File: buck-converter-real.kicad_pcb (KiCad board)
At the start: 4 copper layers, 64 x 64 mm, 75 parts, among them J1 Conn_01x02_Pin, J1 USB_C_Receptacle_USB2.0_16P, J10 I2C1, J12 Conn_01x04, J13 Conn_01x12, J2 SOL 24V, J3 Battery out (3V6-4V2) NiMH 3S, J5 Barrel_Jack_MountingPin, J6 DM3CS-SF, J7 UART 1, J8 I2C1, J9 SWD, Q2 CSD18540Q5B - 60-V, SW2 SW_Omron_B3FS, U1 AP2112K-3.3 (3V3 LDO), U2 CH32V203K8T6, U5 LM5109BMA (Mosfet Driver), U6 78L12L (12V LDO) (35V max), Y1 8MHz 20pF

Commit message: Update layout
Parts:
- added REF**: Untitled, forest-ch:Untitled, F.Cu at (113.8, 70.5)
- added REF**1: Untitled, forest-ch:Untitled, F.Cu at (116.4, 70.5)
- added REF**10: Untitled, forest-ch:Untitled, F.Cu at (124.0, 73.1)
- added REF**12: Untitled, forest-ch:Untitled, F.Cu at (113.8, 75.6)
- added REF**13: Untitled, forest-ch:Untitled, F.Cu at (116.4, 75.6)
- added REF**14: Untitled, forest-ch:Untitled, F.Cu at (118.9, 75.6)
- added REF**15: Untitled, forest-ch:Untitled, F.Cu at (121.5, 75.6)
- added REF**16: Untitled, forest-ch:Untitled, F.Cu at (124.0, 75.6)
- added REF**17: Untitled, forest-ch:Untitled, F.Cu at (126.5, 75.6)
- added REF**18: Untitled, forest-ch:Untitled, F.Cu at (113.8, 78.2)
- added REF**19: Untitled, forest-ch:Untitled, F.Cu at (116.4, 78.2)
- added REF**2: Untitled, forest-ch:Untitled, F.Cu at (118.9, 70.5)
- added REF**20: Untitled, forest-ch:Untitled, F.Cu at (118.9, 78.2)
- added REF**21: Untitled, forest-ch:Untitled, F.Cu at (121.5, 78.2)
- added REF**22: Untitled, forest-ch:Untitled, F.Cu at (124.0, 78.2)
- added REF**23: Untitled, forest-ch:Untitled, F.Cu at (126.5, 78.2)
- added REF**24: Untitled, forest-ch:Untitled, F.Cu at (113.8, 80.7)
- added REF**25: Untitled, forest-ch:Untitled, F.Cu at (116.4, 80.7)
- added REF**26: Untitled, forest-ch:Untitled, F.Cu at (118.9, 80.7)
- added REF**27: Untitled, forest-ch:Untitled, F.Cu at (121.5, 80.7)
- added REF**28: Untitled, forest-ch:Untitled, F.Cu at (124.0, 80.7)
- added REF**29: Untitled, forest-ch:Untitled, F.Cu at (126.5, 80.7)
- added REF**3: Untitled, forest-ch:Untitled, F.Cu at (121.5, 70.5)
- added REF**30: Untitled, forest-ch:Untitled, F.Cu at (113.8, 83.2)
- added REF**31: Untitled, forest-ch:Untitled, F.Cu at (116.4, 83.2)
- added REF**32: Untitled, forest-ch:Untitled, F.Cu at (118.9, 83.2)
- added REF**33: Untitled, forest-ch:Untitled, F.Cu at (121.5, 83.2)
- added REF**34: Untitled, forest-ch:Untitled, F.Cu at (124.0, 83.2)
- added REF**35: Untitled, forest-ch:Untitled, F.Cu at (126.5, 83.2)
- added REF**36: Untitled, forest-ch:Untitled, F.Cu at (113.8, 85.8)
- added REF**37: Untitled, forest-ch:Untitled, F.Cu at (116.4, 85.8)
- added REF**38: Untitled, forest-ch:Untitled, F.Cu at (118.9, 85.8)
- added REF**39: Untitled, forest-ch:Untitled, F.Cu at (121.5, 85.8)
- added REF**4: Untitled, forest-ch:Untitled, F.Cu at (124.0, 70.5)
- added REF**40: Untitled, forest-ch:Untitled, F.Cu at (124.0, 85.8)
- added REF**41: Untitled, forest-ch:Untitled, F.Cu at (126.5, 85.8)
- added REF**42: Untitled, forest-ch:Untitled, F.Cu at (113.8, 88.3)
- added REF**43: Untitled, forest-ch:Untitled, F.Cu at (116.4, 88.3)
- added REF**44: Untitled, forest-ch:Untitled, F.Cu at (118.9, 88.3)
- added REF**45: Untitled, forest-ch:Untitled, F.Cu at (121.5, 88.3)
- added REF**46: Untitled, forest-ch:Untitled, F.Cu at (124.0, 88.3)
- added REF**47: Untitled, forest-ch:Untitled, F.Cu at (126.5, 88.3)
- added REF**48: Untitled, forest-ch:Untitled, F.Cu at (113.8, 90.9)
- added REF**49: Untitled, forest-ch:Untitled, F.Cu at (116.4, 90.9)
- added REF**50: Untitled, forest-ch:Untitled, F.Cu at (118.9, 90.9)
- added REF**51: Untitled, forest-ch:Untitled, F.Cu at (121.5, 90.9)
- added REF**52: Untitled, forest-ch:Untitled, F.Cu at (124.0, 90.9)
- added REF**53: Untitled, forest-ch:Untitled, F.Cu at (126.5, 90.9)
- added REF**54: Untitled, forest-ch:Untitled, F.Cu at (113.8, 93.4)
- added REF**55: Untitled, forest-ch:Untitled, F.Cu at (116.4, 93.4)
- added REF**56: Untitled, forest-ch:Untitled, F.Cu at (118.9, 93.4)
- added REF**57: Untitled, forest-ch:Untitled, F.Cu at (121.5, 93.4)
- added REF**58: Untitled, forest-ch:Untitled, F.Cu at (124.0, 93.4)
- added REF**59: Untitled, forest-ch:Untitled, F.Cu at (126.5, 93.4)
- added REF**6: Untitled, forest-ch:Untitled, F.Cu at (113.8, 73.1)
- added REF**60: Untitled, forest-ch:Untitled, F.Cu at (113.8, 96.0)
- added REF**61: Untitled, forest-ch:Untitled, F.Cu at (116.4, 96.0)
- added REF**62: Untitled, forest-ch:Untitled, F.Cu at (118.9, 96.0)
- added REF**63: Untitled, forest-ch:Untitled, F.Cu at (121.5, 96.0)
- added REF**64: Untitled, forest-ch:Untitled, F.Cu at (124.0, 96.0)
- added REF**65: Untitled, forest-ch:Untitled, F.Cu at (126.5, 96.0)
- added REF**7: Untitled, forest-ch:Untitled, F.Cu at (116.4, 73.1)
- added REF**8: Untitled, forest-ch:Untitled, F.Cu at (118.9, 73.1)
- added REF**9: Untitled, forest-ch:Untitled, F.Cu at (121.5, 73.1)
- moved C14 17.3 mm to (100.2, 102.5), turned to 0 degrees
- moved C12 12.6 mm to (96.0, 97.0), turned to 90 degrees
- moved U1 8.98 mm to (96.5, 101.5)
- moved R30 6.88 mm to (105.0, 80.8)
- moved R31 4.37 mm to (105.0, 76.8), turned to -90 degrees
- moved R27 3.35 mm to (100.5, 93.5)
- moved R28 3.35 mm to (100.5, 97.5)
- moved R29 3.34 mm to (83.5, 78.0), turned to 0 degrees
- moved J12 3.26 mm to (104.0, 91.7)
- moved R17 3.25 mm to (74.8, 78.0)
- moved R18 3.25 mm to (70.8, 78.0)
- moved R19 3.25 mm to (78.8, 78.0)
- moved J10 2.25 mm to (109.5, 78.8)
- moved J7 2.25 mm to (110.2, 84.7)
- moved J8 2.25 mm to (109.5, 95.8)
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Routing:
- net Net-(SMA-915/433MHz1-In): track 6.11 -> 4.86 mm

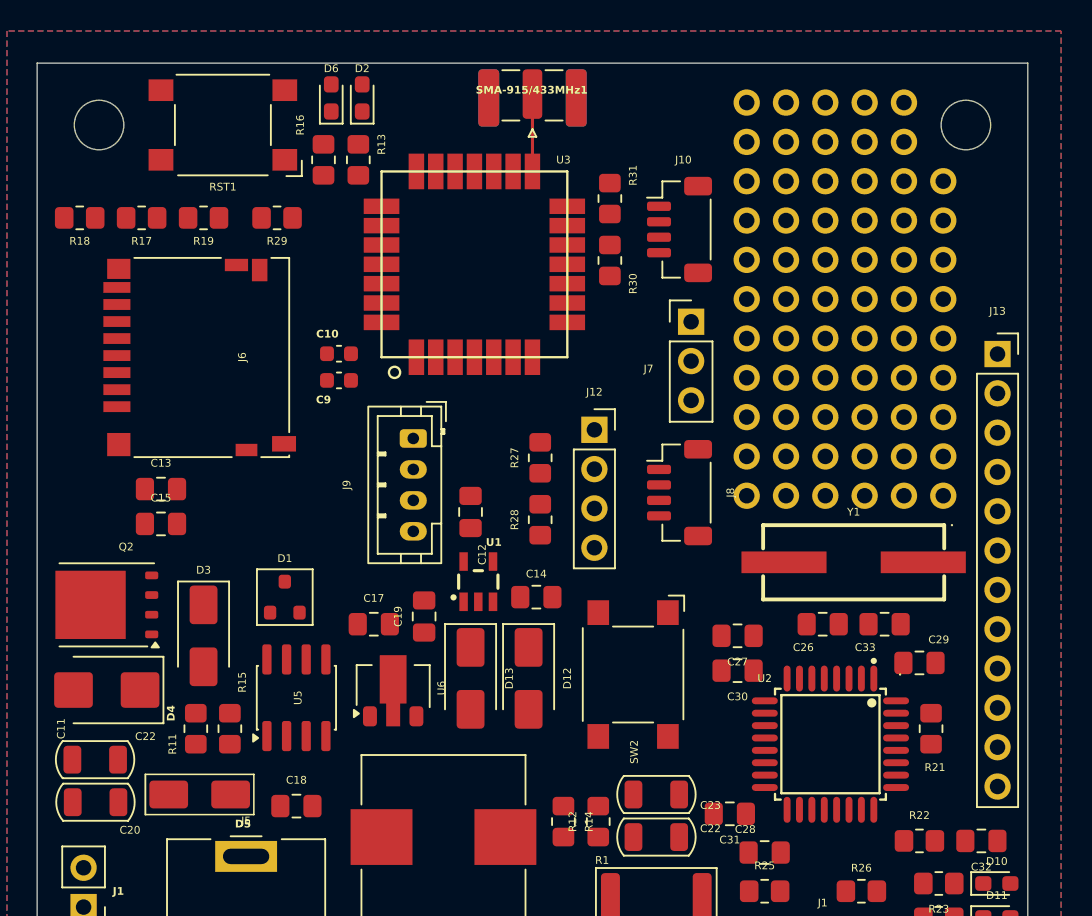
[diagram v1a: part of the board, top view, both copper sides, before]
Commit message: Update layout - add header markings
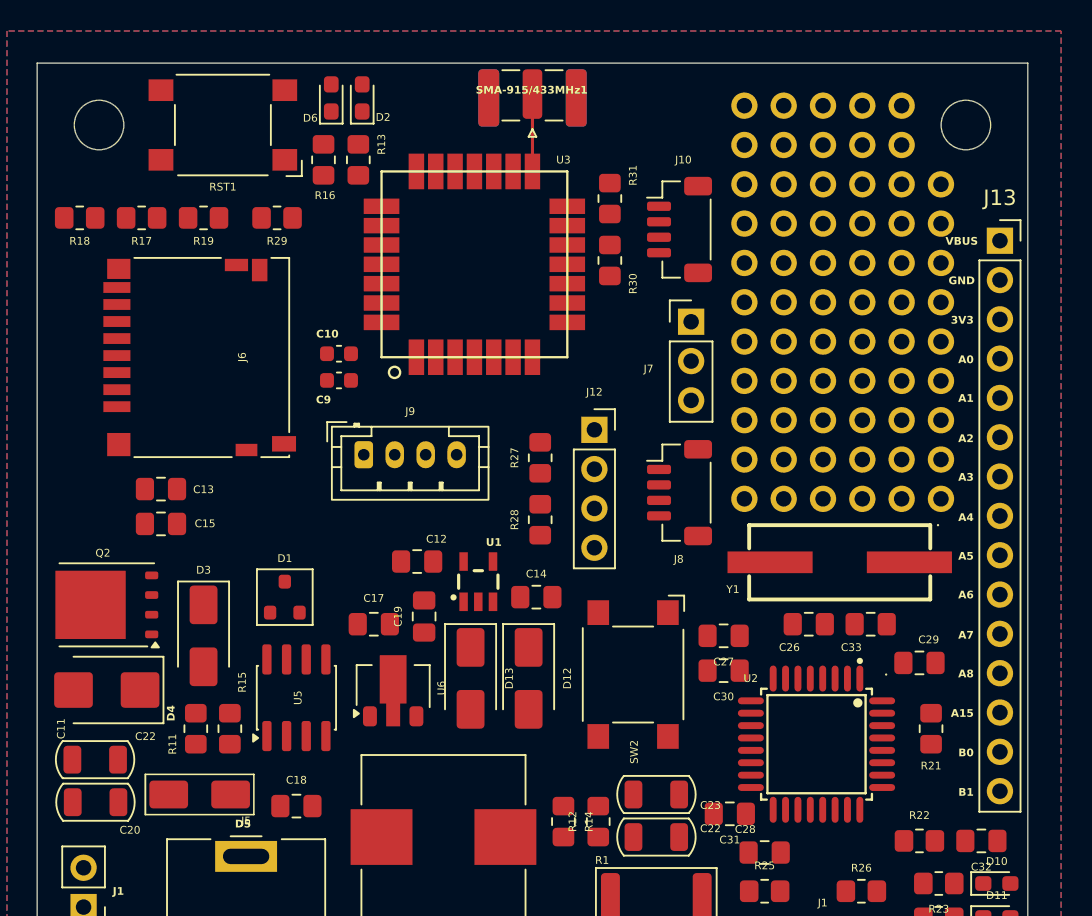
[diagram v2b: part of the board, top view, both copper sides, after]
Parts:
- J13: value Conn_01x12 -> Conn_01x15; footprint Connector_PinSocket_2.54mm:PinSocket_1x12_P2.54mm_Vertical -> Connector_PinSocket_2.54mm:PinSocket_1x15_P2.54mm_Vertical
- moved J13 7.32 mm to (130.2, 79.5)
- moved C12 4.71 mm to (92.5, 100.2), turned to 180 degrees
- moved J9 3.37 mm to (89.1, 93.3), turned to 0 degrees
- moved C26 0.90 mm to (117.8, 104.2)
- moved C27 0.90 mm to (112.3, 105.0)
- moved C30 0.90 mm to (112.3, 107.2)
- moved C33 0.90 mm to (121.8, 104.2)
- moved U2 0.90 mm to (118.3, 112.0)
- moved Y1 0.90 mm to (119.8, 100.2)
- moved REF** 0.25 mm to (113.7, 70.8)
- moved REF**10 0.25 mm to (123.8, 73.3)
- moved REF**12 0.25 mm to (113.7, 75.8)
- moved REF**14 0.25 mm to (118.8, 75.8)
- moved REF**16 0.25 mm to (123.8, 75.8)
- moved REF**17 0.25 mm to (126.4, 75.8)
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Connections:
- J13 pad 1: Net-(J13-Pin_1) -> VBUS
- J13 pad 2: Net-(J13-Pin_2) -> GND
- J13 pad 3: Net-(J13-Pin_3) -> +3.3V
- U2 pad 10: Net-(J13-Pin_5) -> Net-(J13-Pin_8)
- U2 pad 11: Net-(J13-Pin_6) -> Net-(J13-Pin_9)
- U2 pad 12: Net-(J13-Pin_7) -> Net-(J13-Pin_10)
- U2 pad 13: Net-(J13-Pin_8) -> Net-(J13-Pin_11)
- U2 pad 14: Net-(J13-Pin_11) -> Net-(J13-Pin_14)
- U2 pad 15: Net-(J13-Pin_12) -> Net-(J13-Pin_15)
- U2 pad 18: Net-(J13-Pin_9) -> Net-(J13-Pin_12)
- U2 pad 25: Net-(J13-Pin_10) -> Net-(J13-Pin_13)
- U2 pad 6: Net-(J13-Pin_1) -> Net-(J13-Pin_4)
- U2 pad 7: Net-(J13-Pin_2) -> Net-(J13-Pin_5)
- U2 pad 8: Net-(J13-Pin_3) -> Net-(J13-Pin_6)
- U2 pad 9: Net-(J13-Pin_4) -> Net-(J13-Pin_7)
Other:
- board text added: "3V3"
- board text added: "A0"
- board text added: "A1"
- board text added: "A15"
- board text added: "A2"
- board text added: "A3"
- board text added: "A4"
- board text added: "A5"
- board text added: "A6"
- board text added: "A7"
- board text added: "A8"
- board text added: "B0"
- board text added: "B1"
- board text added: "VBUS"

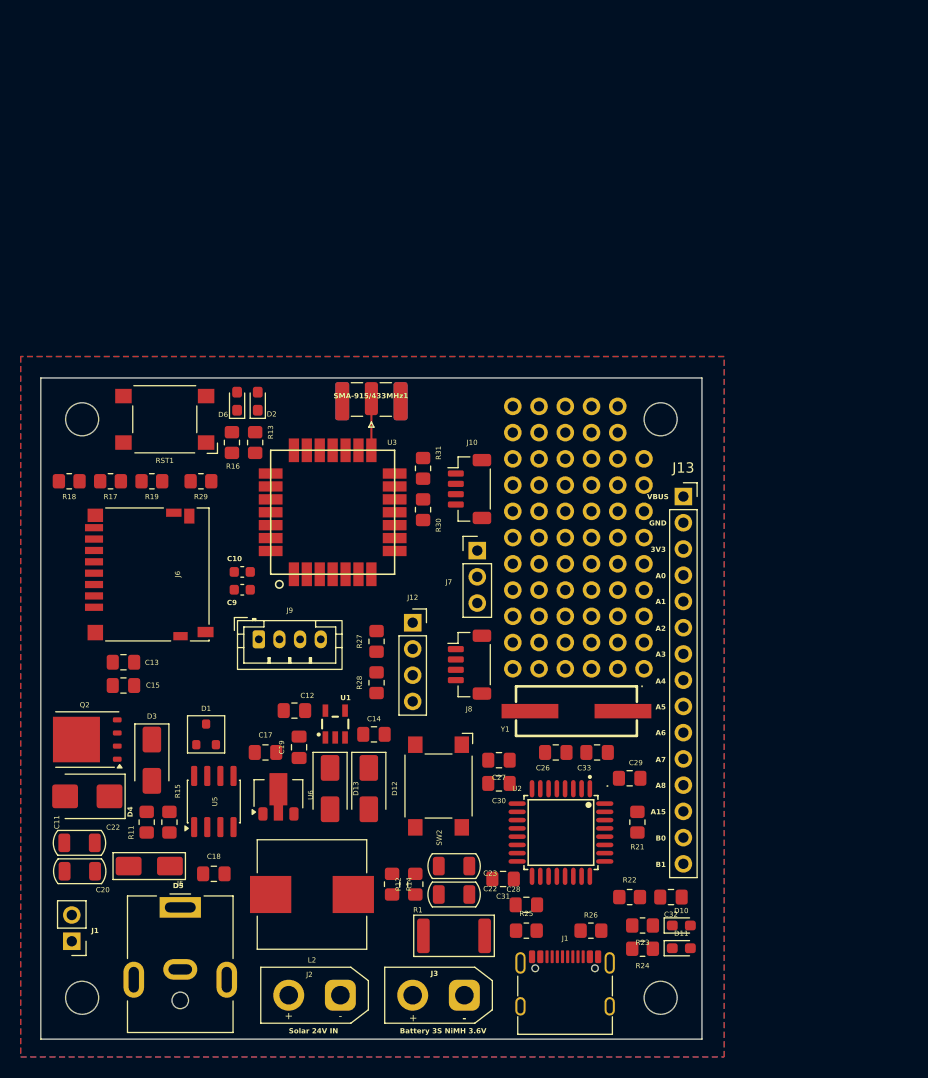
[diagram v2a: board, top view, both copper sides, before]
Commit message: Update layout - fully routed
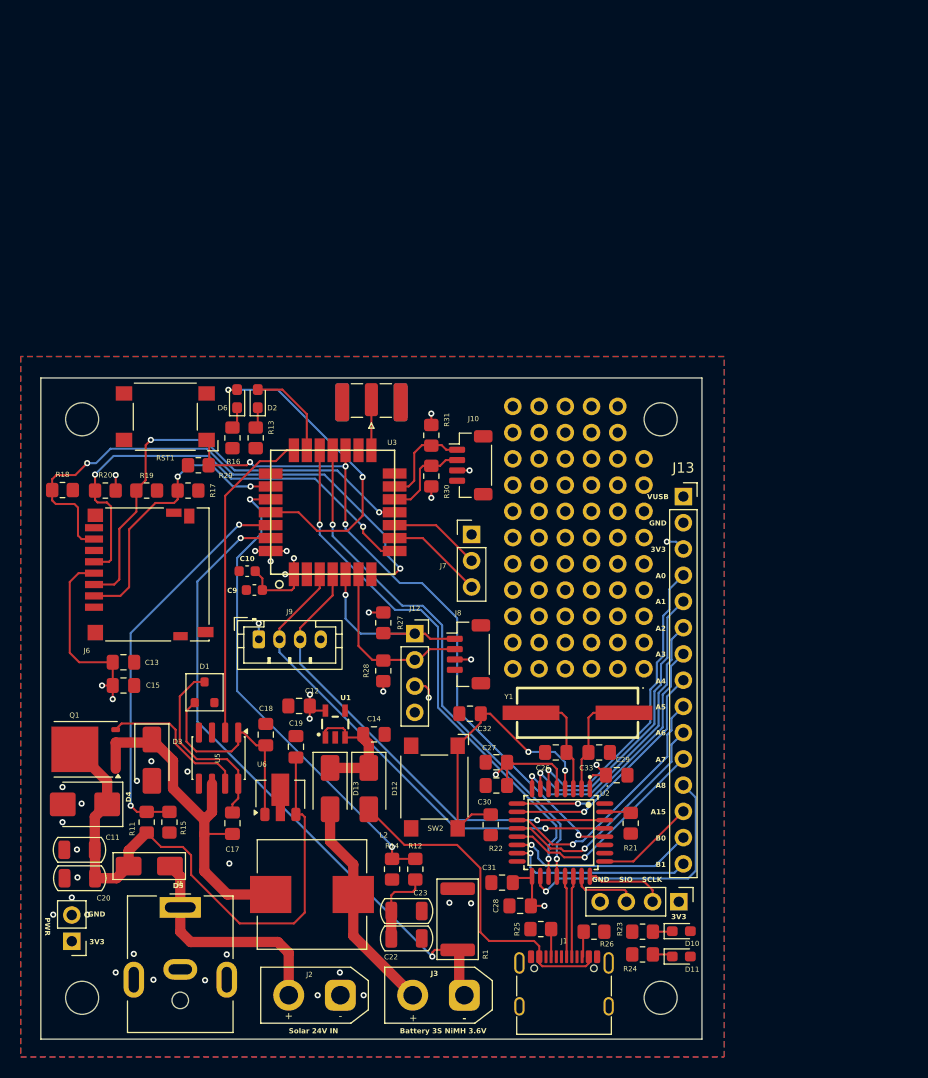
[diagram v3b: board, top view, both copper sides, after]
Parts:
- removed Q2: CSD18540Q5B - 60-V, Package_TO_SOT_SMD:TDSON-8-1
- added J11: SWD, Connector_PinHeader_2.54mm:PinHeader_1x04_P2.54mm_Vertical, F.Cu at (129.8, 118.7)
- added Q1: CSD18540Q5B - 60-V, Package_TO_SOT_SMD:TDSON-8-1, F.Cu at (72.3, 103.9)
- added R20: 10K, Resistor_SMD:R_0805_2012Metric_Pad1.20x1.40mm_HandSolder, F.Cu at (74.2, 78.9)
- moved C32 26.3 mm to (109.5, 100.5), turned to 0 degrees
- moved R22 15.2 mm to (111.5, 111.2), turned to 90 degrees
- moved C18 14.4 mm to (89.8, 102.5), turned to 90 degrees
- moved C17 7.56 mm to (86.5, 111.1), turned to 90 degrees
- moved R17 7.55 mm to (82.2, 78.9), turned to 180 degrees
- moved C23 6.33 mm to (103.4, 119.6)
- moved C22 6.26 mm to (103.4, 122.2)
- moved U5 4.22 mm to (85.2, 104.8), turned to -90 degrees
- moved D1 4.08 mm to (83.8, 98.4)
- moved R30 3.35 mm to (105.8, 77.5)
- moved R31 3.30 mm to (105.8, 73.5)
- moved J10 2.30 mm to (109.6, 76.5)
- moved R27 1.91 mm to (101.2, 91.7), turned to -90 degrees
- moved J7 1.65 mm to (109.7, 83.2)
- moved R1 1.64 mm to (108.3, 120.4), turned to -90 degrees
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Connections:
- D12 pad 2: Net-(D12-A) -> VBUS
- J1 pad A4: Net-(D12-A) -> VBUS
- J1 pad A9: Net-(D12-A) -> VBUS
- J1 pad B4: Net-(D12-A) -> VBUS
- J1 pad B9: Net-(D12-A) -> VBUS
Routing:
- net +3.3V: track 0.00 -> 71.5 mm, vias 0 -> 22
- net /WIO-RST: track 0.00 -> 66.3 mm, vias 0 -> 4
- net /BAT_ISENSE: track 0.00 -> 61.8 mm, vias 0 -> 2
- net /Solar In: track 0.00 -> 58.2 mm
- net /SPI-CITO: track 0.00 -> 53.0 mm, vias 0 -> 2
- net /UART-WIO-TX: track 0.00 -> 52.5 mm, vias 0 -> 2
- net /UART-WIO-RX: track 0.00 -> 51.6 mm, vias 0 -> 2
- net /VSENSE_VOUT: track 0.00 -> 48.1 mm, vias 0 -> 2
- net /SWD-WIO-IO: track 0.00 -> 47.7 mm, vias 0 -> 1
- net /SWD-WIO-CLK: track 0.00 -> 45.7 mm, vias 0 -> 1
- net /SPI-SCK: track 0.00 -> 45.1 mm, vias 0 -> 2
- net /SPI-COTI: track 0.00 -> 43.9 mm, vias 0 -> 2
- net /VSENSE_VIN: track 0.00 -> 38.6 mm, vias 0 -> 2
- net Net-(D3-K): track 0.00 -> 34.9 mm
- net VBUS: track 0.00 -> 32.9 mm
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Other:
- board text added: "PWR"
- board text added: "SCLK"
- board text added: "SIO"
- board text added: "VUSB"
- board text removed: "C22"
- board text removed: "VBUS"

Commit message: Update layout - v1
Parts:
- added J14: Boot, Connector_PinHeader_2.54mm:PinHeader_1x02_P2.54mm_Vertical, F.Cu at (109.8, 114.5)
- added R32: 10K, Resistor_SMD:R_0805_2012Metric_Pad1.20x1.40mm_HandSolder, F.Cu at (83.0, 95.2)
- added RST2: SW_Omron_B3FS, Button_Switch_SMD:SW_SPST_Omron_B3FS-100xP, F.Cu at (76.0, 97.5)
- moved C13 7.22 mm to (69.7, 99.0), turned to -90 degrees
- moved C15 6.82 mm to (69.7, 95.2), turned to -90 degrees
- moved R22 0.70 mm to (111.8, 110.6)
- moved D6 0.45 mm to (86.5, 70.0)
- moved R21 0.41 mm to (124.7, 111.0)
- moved D3 0.30 mm to (78.8, 105.3)
- moved D2 0.20 mm to (88.8, 70.0)
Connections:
- D10 pad 2: unconnected-(D10-A-Pad2) -> Net-(D10-A)
- D11 pad 2: unconnected-(D11-A-Pad2) -> Net-(D11-A)
- U2 pad 26: unconnected-(U2-PB3-Pad26) -> Net-(D11-A)
- U2 pad 27: unconnected-(U2-PB4-Pad27) -> Net-(D10-A)
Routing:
- net VBUS: track 32.9 -> 87.7 mm
- net /LED1: track 31.5 -> 70.6 mm, vias 2 -> 4
- net Net-(J14-Pin_2): track 2.55 -> 29.3 mm, vias 0 -> 2
- net +3.3V: track 71.5 -> 90.3 mm, vias 22 -> 33
- net Net-(D11-A): track 0.00 -> 17.7 mm
- net Net-(D10-A): track 0.00 -> 15.0 mm
- net Net-(R32-Pad2): track 0.00 -> 10.2 mm
- net /WIO-RST: track 66.3 -> 75.5 mm
- net Net-(U2-PA11/USB1DM): track 7.85 -> 10.6 mm
- net Net-(U2-PA12/USB1DP): track 7.85 -> 10.5 mm
- net +BATT: track 29.0 -> 27.6 mm
- net Net-(J13-Pin_14): track 18.5 -> 19.8 mm
- net Net-(J13-Pin_11): track 20.9 -> 21.7 mm
- net Net-(J13-Pin_10): track 22.7 -> 23.5 mm
- net /SPI-COTI: track 43.9 -> 44.7 mm
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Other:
- board text added: "BOOT"
- board text added: "I2C1"
- board text added: "I2C2"
- board text added: "RESET"
- board text added: "RESET RF"
- board text added: "RX"
- board text added: "SCL"
- board text added: "SDA"
- board text added: "SMA"
- board text added: "SWD"
- board text added: "TX"
- board text added: "UART"
- board text added: "UB"

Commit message: Update schematic/layout - minor cosmetics
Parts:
- moved C28 1.41 mm to (113.0, 119.5)
- moved C31 0.68 mm to (113.0, 117.4)
- moved R25 0.14 mm to (116.5, 121.5)
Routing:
- net +3.3V: track 90.3 -> 94.2 mm
- net GND: vias 145 -> 159
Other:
- board text added: "3V3 PWR"
- board text removed: "PWR"

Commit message: Update layout - minor tweaks
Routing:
- net Net-(J14-Pin_2): track 29.3 -> 32.7 mm
- net /VSENSE_VOUT: track 48.5 -> 46.9 mm
- net VBUS: track 87.7 -> 89.1 mm
- net +3.3V: track 94.2 -> 93.3 mm
